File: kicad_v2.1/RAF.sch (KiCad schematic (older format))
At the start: 40 parts, among them J1 SERVO, J2 SERVO, J3 SOL, J4 SERVO, J5 PUMP, J6 WS2811-OUT, J7 I2C, P1 Power, P2 Analog, P3 Digital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

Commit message: RAF v2.1 kicad layout
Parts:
- D1, D2: value SD3220 -> S1ATR
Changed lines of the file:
@@
 P 9025 1025
 F 0 "D1" V 8950 1050 50  0000 L CNN
-F 1 "SD3220" V 9100 700 50  0000 L CNN
+F 1 "S1ATR" V 9100 700 50  0000 L CNN
 F 2 "RAF_Libs:SMA_Handsoldering" V 9025 1025 50  0001 C CNN
 F 3 "" V 9025 1025 50  0000 C CNN
@@
 P 9025 2525
 F 0 "D2" V 8950 2550 50  0000 L CNN
-F 1 "SD3220" V 9100 2200 50  0000 L CNN
+F 1 "S1ATR" V 9100 2200 50  0000 L CNN
 F 2 "RAF_Libs:SMA_Handsoldering" V 9025 2525 50  0001 C CNN
 F 3 "" V 9025 2525 50  0000 C CNN

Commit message: LDR footprint modified
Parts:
- LDR1: footprint RAF_Libs:Resistor_LDR_4.9x4.2_RM2.54 -> RAF_Libs:Resistor_LDR_5.0x3.4
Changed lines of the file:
@@
 F 0 "LDR1" H 2250 3525 40  0000 L CNB
 F 1 "LIGHT" H 2250 3475 40  0000 L TNB
-F 2 "RAF_Libs:Resistor_LDR_4.9x4.2_RM2.54" V 2375 3450 50  0001 C CNN
+F 2 "RAF_Libs:Resistor_LDR_5.0x3.4" V 2375 3450 50  0001 C CNN
 F 3 "" H 2200 3400 50  0000 C CNN
 F 4 "Value" H 2200 3450 60  0001 C CNN "manf#"

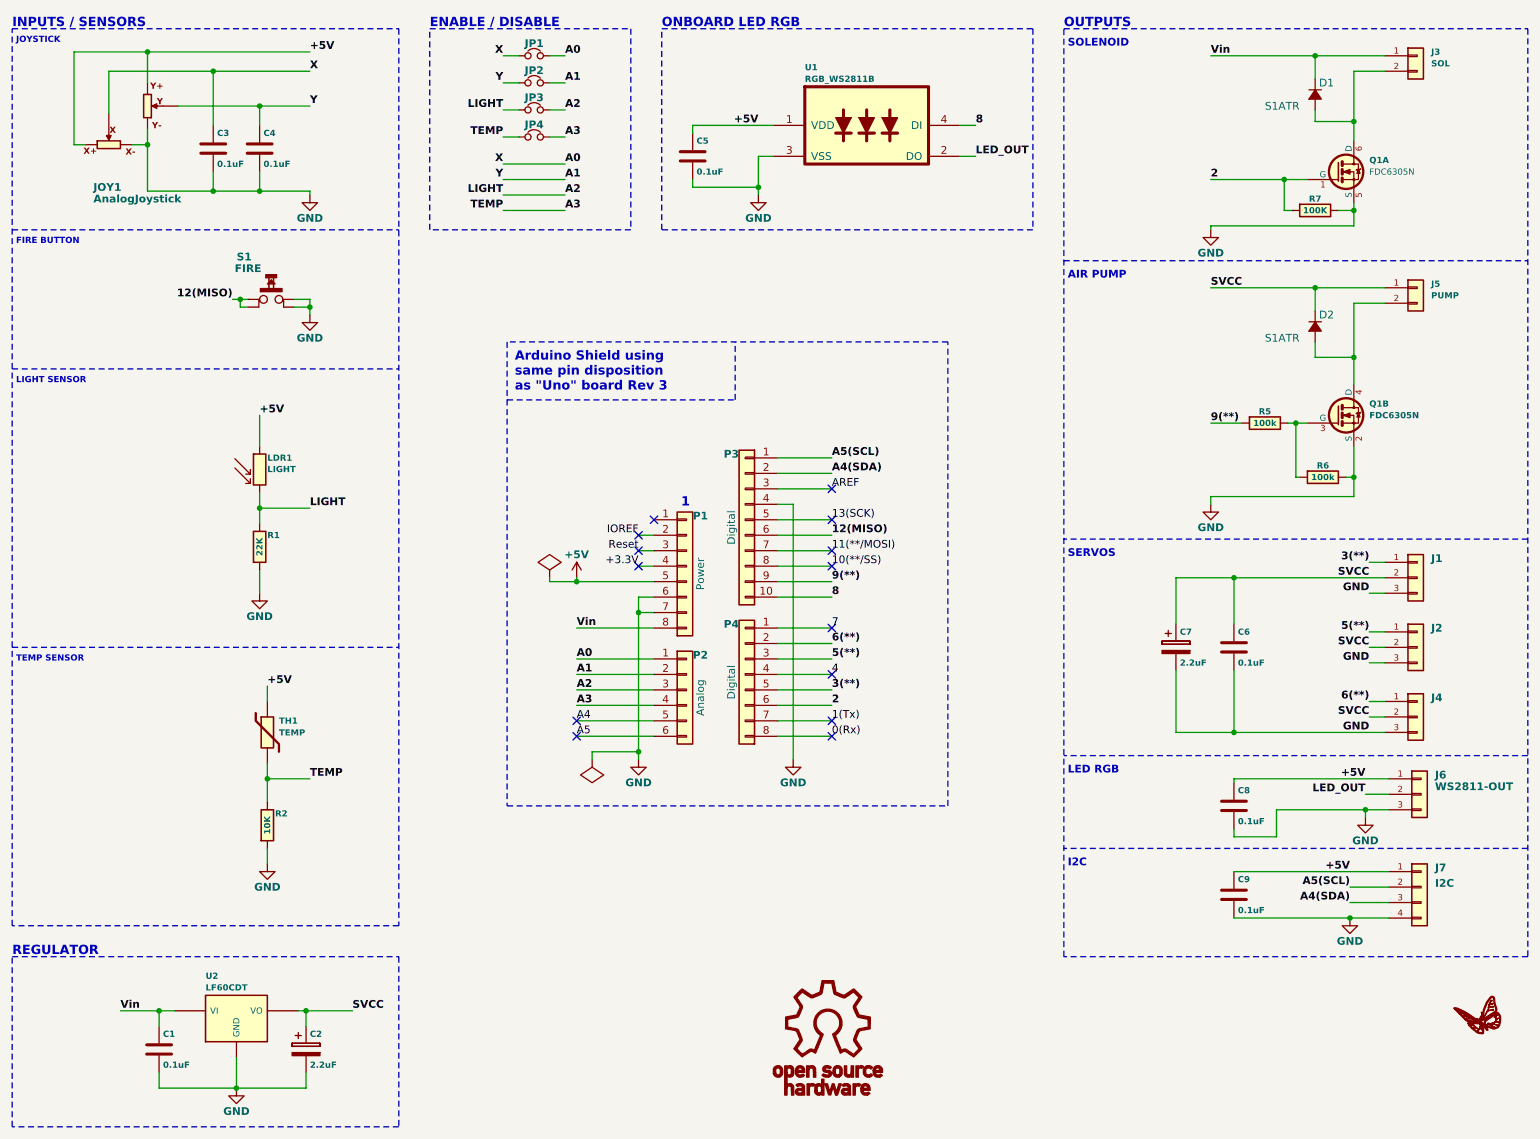
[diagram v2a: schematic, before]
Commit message: PCB ver2.1 complete, added variable resistor for LDR
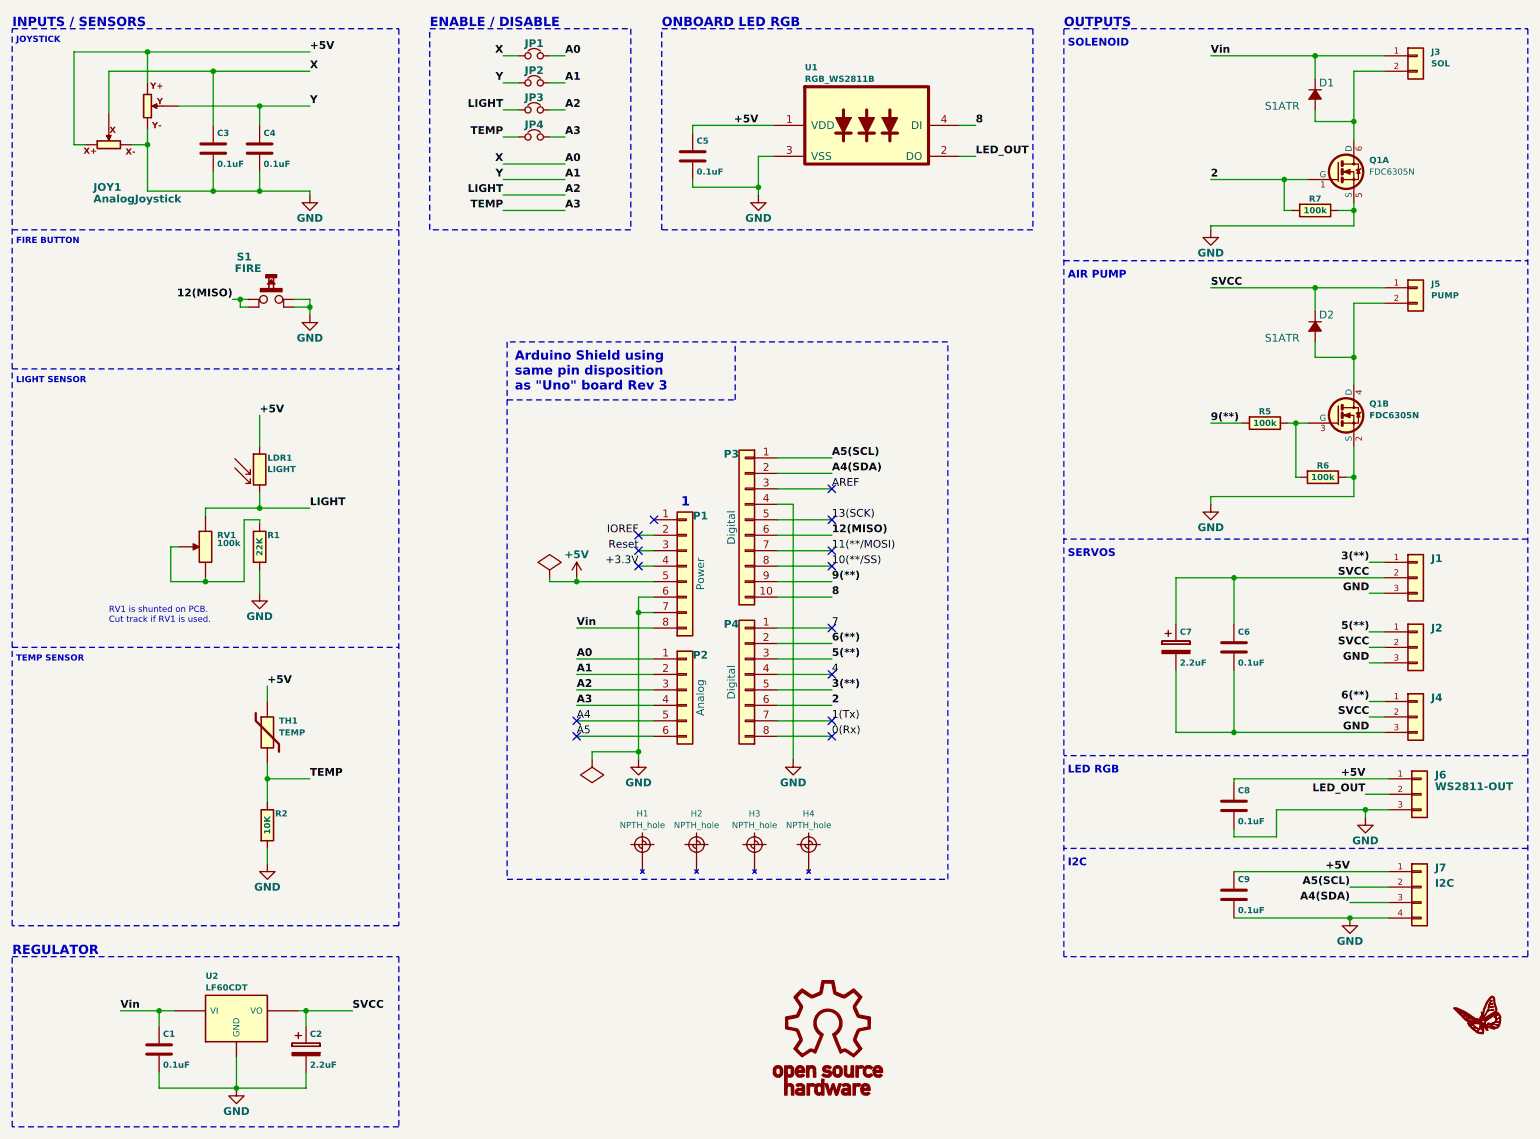
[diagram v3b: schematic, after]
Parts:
- added H1, H2, H3, H4: NPTH_hole, RAF_Libs:NPTH_hole_3mm, symbol NPTH_hole
- added RV1: 100k, RAF_Libs:Res_variable, symbol Res_variable
- R7: value 100K -> 100k
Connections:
- net A2: now also RV1.1; no longer R1.1
- new net: R1.1, RV1.2, RV1.3
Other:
- note added: "RV1 is shunted on PCB.\nCut track if RV1 is used."
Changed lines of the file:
@@
 Title "Ready Aim Fire Shield"
 Date "2017-08-24"
-Rev "V2.0"
+Rev "V2.1"
 Comp ""
 Comment1 ""
@@
 P 9025 1775
 F 0 "R7" V 8950 1775 40  0000 C CNB
-F 1 "100K" V 9025 1775 40  0000 C CNB
+F 1 "100k" V 9025 1775 40  0000 C CNB
 F 2 "RAF_Libs:R_0805_HandSoldering" V 8955 1775 50  0001 C CNN
 F 3 "" H 9025 1775 50  0001 C CNN
@@
 	4750 3975 4650 3975
 Wire Wire Line
-	2200 3600 2200 3800
-Wire Wire Line
-	2200 3700 2525 3700
+	1850 3700 2525 3700
 Connection ~ 2200 3700
 Wire Wire Line
@@
 	6650 2625 3800 2625
 Wire Notes Line
-	3800 2625 3800 5625
-Wire Notes Line
-	3800 5625 6650 5625
-Wire Notes Line
-	6650 5625 6650 2625
+	3800 2625 3800 6100
+Wire Notes Line
+	3800 6100 6650 6100
+Wire Notes Line
+	6650 6100 6650 2625
 Wire Wire Line
 	8500 5450 9500 5450
@@
 Wire Wire Line
 	8125 4150 9475 4150
+$Comp
+L NPTH_hole H1
+U 1 1 59A15335
+P 4675 5875
+F 0 "H1" H 4675 6075 40  0000 C CNN
+F 1 "NPTH_hole" H 4675 6000 40  0000 C CNN
+F 2 "RAF_Libs:NPTH_hole_3mm" H 4675 5875 50  0001 C CNN
+F 3 "" H 4675 5875 50  0001 C CNN
+	1    4675 5875
+	1    0    0    -1
+$EndComp
+$Comp
+L NPTH_hole H2
+U 1 1 59A15906
+P 5025 5875
+F 0 "H2" H 5025 6075 40  0000 C CNN
+F 1 "NPTH_hole" H 5025 6000 40  0000 C CNN
+F 2 "RAF_Libs:NPTH_hole_3mm" H 5025 5875 50  0001 C CNN
+F 3 "" H 5025 5875 50  0001 C CNN
+	1    5025 5875
+	1    0    0    -1
+$EndComp
+$Comp
+L NPTH_hole H3
+U 1 1 59A15979
+P 5400 5875
+F 0 "H3" H 5400 6075 40  0000 C CNN
+F 1 "NPTH_hole" H 5400 6000 40  0000 C CNN
+F 2 "RAF_Libs:NPTH_hole_3mm" H 5400 5875 50  0001 C CNN
+F 3 "" H 5400 5875 50  0001 C CNN
+	1    5400 5875
+	1    0    0    -1
+$EndComp
+$Comp
+L NPTH_hole H4
+U 1 1 59A159E2
+P 5750 5875
+F 0 "H4" H 5750 6075 40  0000 C CNN
+F 1 "NPTH_hole" H 5750 6000 40  0000 C CNN
+F 2 "RAF_Libs:NPTH_hole_3mm" H 5750 5875 50  0001 C CNN
+F 3 "" H 5750 5875 50  0001 C CNN
+	1    5750 5875
+	1    0    0    -1
+$EndComp
+$Comp
+L Res_variable RV1
+U 1 1 59A162CA
+P 1850 3950
+F 0 "RV1" H 1925 4025 40  0000 L CNB
+F 1 "100k" H 1925 3950 40  0000 L BNB
+F 2 "RAF_Libs:Res_variable" H 1850 3950 50  0001 C CNN
+F 3 "" H 1850 3950 50  0001 C CNN
+F 4 "Value" H 1850 3950 50  0001 C CNN "manf#"
+	1    1850 3950
+	1    0    0    -1
+$EndComp
+Wire Wire Line
+	1850 3700 1850 3750
+Wire Wire Line
+	1675 3950 1625 3950
+Wire Wire Line
+	1625 3950 1625 4175
+Wire Wire Line
+	1625 4175 2100 4175
+Wire Wire Line
+	1850 4175 1850 4150
+Wire Wire Line
+	2200 3600 2200 3700
+Wire Wire Line
+	2200 3800 2200 3775
+Wire Wire Line
+	2200 3775 2100 3775
+Wire Wire Line
+	2100 3775 2100 4175
+Connection ~ 1850 4175
+Text Notes 1225 4450 0    40   ~ 0
+RV1 is shunted on PCB.\nCut track if RV1 is used.
 $EndSCHEMATC

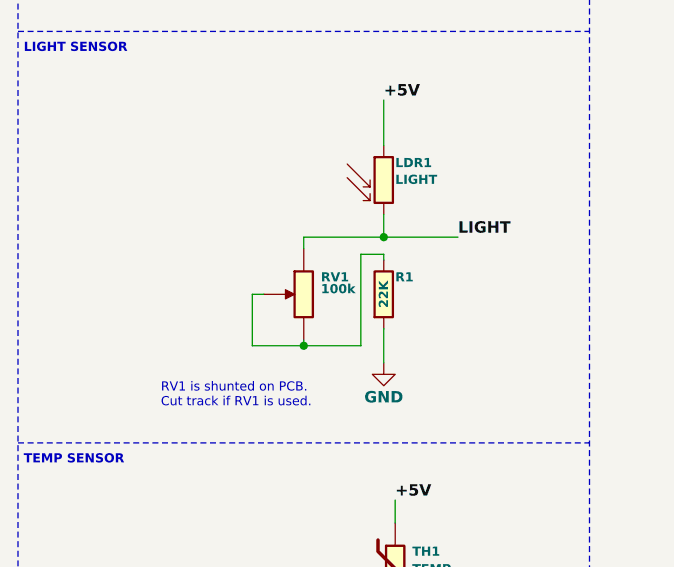
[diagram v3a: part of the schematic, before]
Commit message: kicad_v2.1 updated silkscreen
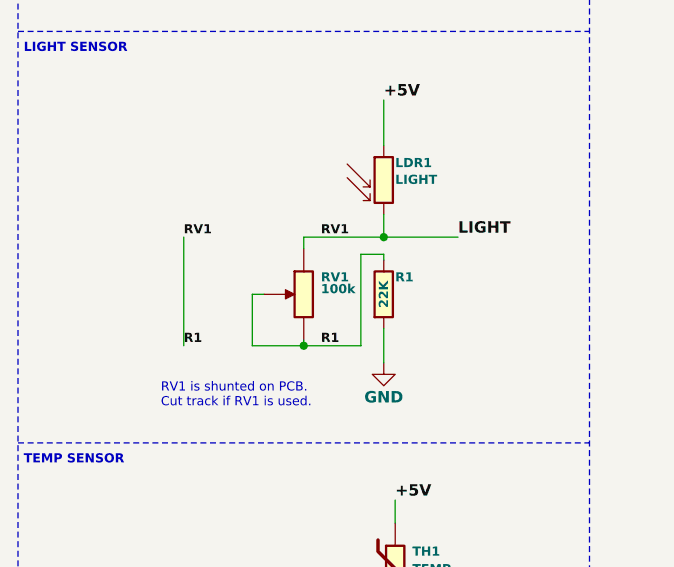
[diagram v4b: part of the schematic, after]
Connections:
- net A2: now also R1.1, RV1.2, RV1.3
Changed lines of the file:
@@
 Text Notes 1225 4450 0    40   ~ 0
 RV1 is shunted on PCB.\nCut track if RV1 is used.
+Text Label 1925 3700 0    40   ~ 8
+RV1
+Text Label 1925 4175 0    40   ~ 8
+R1
+Wire Wire Line
+	1325 3700 1325 4175
+Text Label 1325 4175 0    40   ~ 8
+R1
+Text Label 1325 3700 0    40   ~ 8
+RV1
 $EndSCHEMATC
